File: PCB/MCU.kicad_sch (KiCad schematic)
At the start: 0 parts

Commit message: Finished the schematic.
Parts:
- added C7: 4.7u, Capacitor_SMD:C_0201_0603Metric, symbol Device:C
- added C8: 100n, Capacitor_SMD:C_0201_0603Metric, symbol Device:C
- added J4: Conn_ST_STDC14, Connector_PinHeader_1.27mm:PinHeader_2x07_P1.27mm_Vertical_SMD, symbol Connector:Conn_ST_STDC14
- added R21, R22: 2k, Resistor_SMD:R_0201_0603Metric, symbol Device:R
- added U4: STM32G031K8U6, Package_DFN_QFN:QFN-32-1EP_5x5mm_P0.5mm_EP3.45x3.45mm, symbol CustomSymbols:STM32G031K8U6
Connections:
- new net +3V3: C7.2, C8.2, R21.1, R22.2, U4.5 (VDD)
- new net ALRT: U4.16 (PB1)
- new net BTN_NEXT: U4.32 (PB8)
- new net BTN_PLAY_PAUSE: U4.15 (PB0)
- new net BTN_PREV: U4.1 (PB9)
- new net DREQ: U4.27 (PB3)
- new net ENC_A: U4.7 (PA0)
- new net ENC_B: U4.8 (PA1)
- new net GND: C7.1, C8.1, J4.11 (GNDDetect), J4.5 (GND), J4.7 (GND), U4.33 (VSS), U4.4 (VSS)
- new net LED_ERROR: U4.20 (PC6)
- new net LED_PAUSED: U4.28 (PB4)
- new net LED_PLAYING: U4.29 (PB5)
- new net MISO: U4.13 (PA6)
- new net MOSI: U4.14 (PA7)
- new net RESET: J4.12 (~{RST}), U4.6 (PF2-NRST)
- new net RX: J4.14 (VCP_TX), U4.10 (PA3)
- new net SCK: U4.12 (PA5)
- new net SCL: R21.2, U4.19 (PA9)
- new net SDA: R22.1, U4.21 (PA10)
- new net SD_CS: U4.11 (PA4)
- new net SWCLK: J4.6 (JCLK/SWCLK), U4.25 (PA14-BOOT0)
- new net SWDIO: J4.4 (JTMS/SWDIO), U4.24 (PA13)
- new net TX: J4.13 (VCP_RX), U4.9 (PA2)
- new net XD_CS: U4.23 (PA12)
- new net X_CS: U4.22 (PA11)
- no-connect marks 0 -> 11

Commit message: fixed schematic errors
Accidentally set all SMD 0603 to SMD 0603 metric
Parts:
- C7, C8: footprint Capacitor_SMD:C_0201_0603Metric -> Capacitor_SMD:C_0603_1608Metric
- R21, R22: footprint Resistor_SMD:R_0201_0603Metric -> Resistor_SMD:R_0603_1608Metric
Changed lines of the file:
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@@
 			)
 		)
-		(property "Footprint" "Capacitor_SMD:C_0201_0603Metric"
+		(property "Footprint" "Capacitor_SMD:C_0603_1608Metric"
 			(at 62.5348 72.39 0)
 			(effects
@@
 			)
 		)
-		(property "Footprint" "Resistor_SMD:R_0201_0603Metric"
+		(property "Footprint" "Resistor_SMD:R_0603_1608Metric"
 			(at 125.222 120.65 90)
 			(effects
@@
 			)
 		)
-		(property "Footprint" "Resistor_SMD:R_0201_0603Metric"
+		(property "Footprint" "Resistor_SMD:R_0603_1608Metric"
 			(at 125.222 104.14 90)
 			(effects
@@
 			)
 		)
-		(property "Footprint" "Capacitor_SMD:C_0201_0603Metric"
+		(property "Footprint" "Capacitor_SMD:C_0603_1608Metric"
 			(at 73.9648 72.39 0)
 			(effects

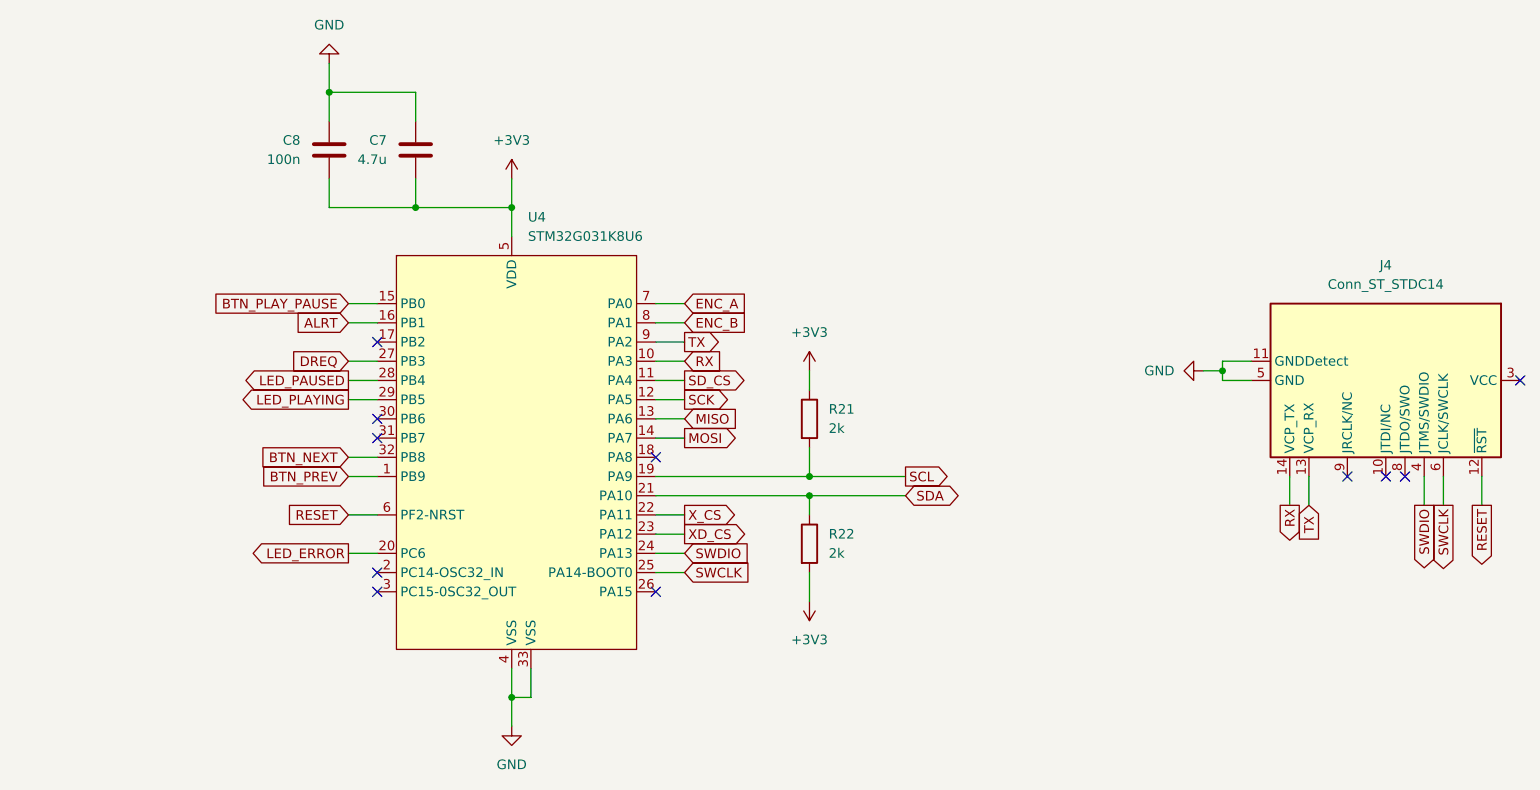
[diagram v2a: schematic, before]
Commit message: Finished initial pcb routing
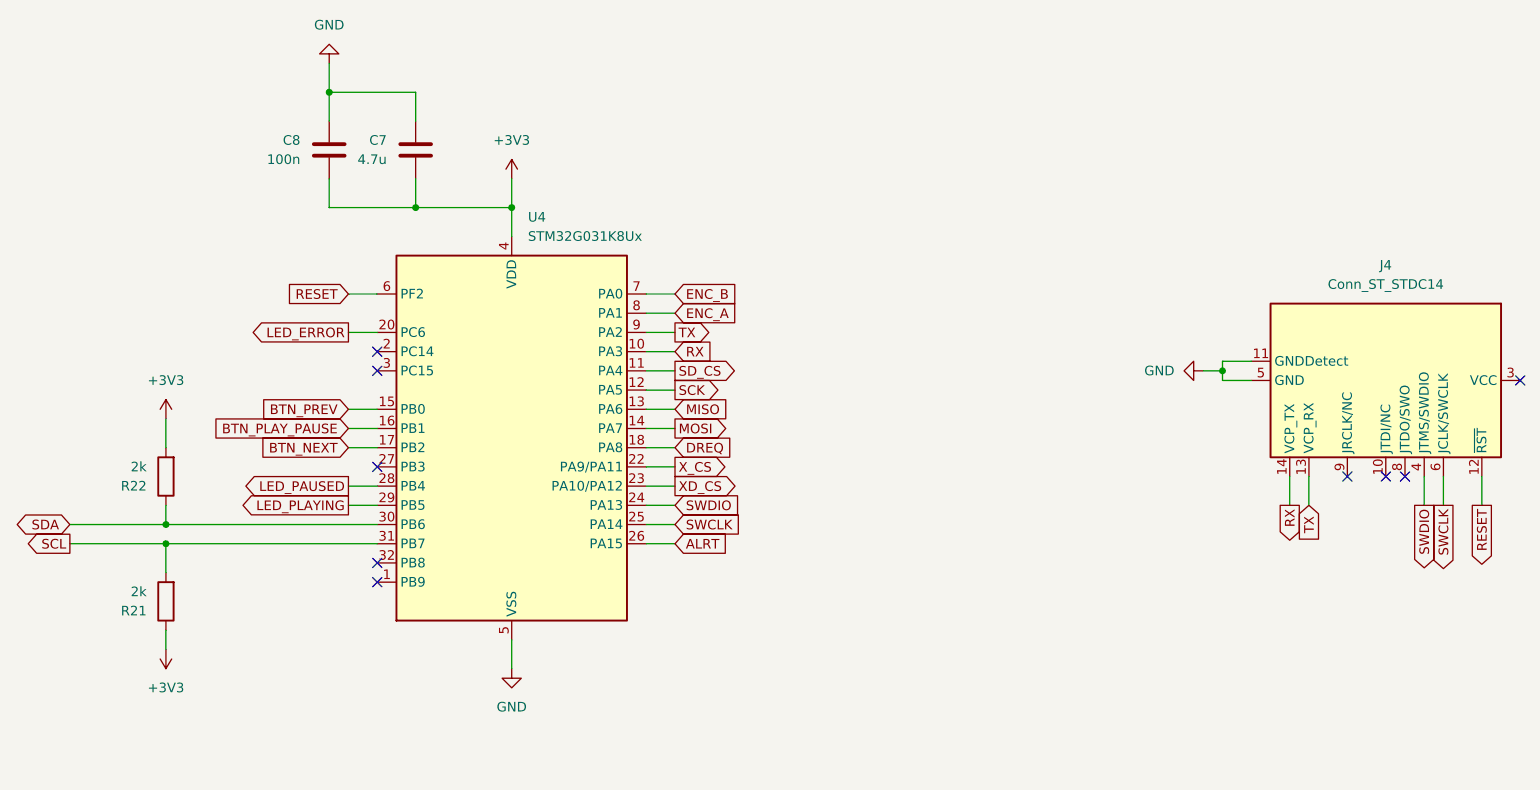
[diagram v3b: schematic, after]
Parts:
- removed U4: STM32G031K8U6, Package_DFN_QFN:QFN-32-1EP_5x5mm_P0.5mm_EP3.45x3.45mm, symbol CustomSymbols:STM32G031K8U6
- added U4: STM32G031K8Ux, Package_DFN_QFN:QFN-32-1EP_5x5mm_P0.5mm_EP3.45x3.45mm, symbol MCU_ST_STM32G0:STM32G031K8Ux
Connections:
- net +3V3: now also U4.4 (VDD)
- net ALRT: now also U4.26 (PA15)
- net BTN_NEXT: now also U4.17 (PB2)
- net BTN_PLAY_PAUSE: now also U4.16 (PB1)
- net BTN_PREV: now also U4.15 (PB0)
- net DREQ: now also U4.18 (PA8)
- net ENC_A: now also U4.8 (PA1)
- net ENC_B: now also U4.7 (PA0)
- net GND: now also U4.33 (VSS), U4.5 (VSS)
- net LED_ERROR: now also U4.20 (PC6)
- net LED_PAUSED: now also U4.28 (PB4)
- net LED_PLAYING: now also U4.29 (PB5)
- net MISO: now also U4.13 (PA6)
- net MOSI: now also U4.14 (PA7)
- net RESET: now also U4.6 (PF2)
- net RX: now also U4.10 (PA3)
- net SCK: now also U4.12 (PA5)
- net SCL: now also U4.31 (PB7)
- net SDA: now also U4.30 (PB6)
- net SD_CS: now also U4.11 (PA4)
- net SWCLK: now also U4.25 (PA14)
- net SWDIO: now also U4.24 (PA13)
- net TX: now also U4.9 (PA2)
- net XD_CS: now also U4.23 (PA10/PA12)
- net X_CS: now also U4.22 (PA9/PA11)
- no-connect marks 11 -> 9
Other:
- moved on the sheet: R21, R22

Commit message: Finished making a PCB for it
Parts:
- U4: LCSC (none) -> C432207
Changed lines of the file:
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@@
+			)
+		)
+		(property "LCSC" "C432207"
+			(at 87.63 107.95 0)
+			(effects
+				(font
+					(size 1.27 1.27)
+				)
+				(hide yes)
 			)
 		)
